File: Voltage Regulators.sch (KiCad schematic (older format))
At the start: 16 parts

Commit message: v1.0
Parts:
- added C?: 10n, symbol C_Small
- added C? (x2): 1u, symbol C_Small
- added U?: NCP700B, TSOT-23-5, symbol NCP700B
- C?: value 22n -> 100n
- R?: value 54.9k -> 43k
- R?: value 5k -> 3.9k
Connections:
- net +15V: now also D?.2 (A), L?.2
- net +3V3: now also C?.1, U?.5 (OUT); no longer C?.1, L?.1, U?.5 (Vin)
- net DC_3V6: now also C?.1, L?.1, U?.5 (Vin), C?.1, U?.1 (IN), U?.3 (EN)
- net GND: now also C?.2, C?.2, C?.2, U?.2 (GND)
- net at C?.2, D?.1 (K), L?.1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: no longer U?.16 (VSW)
- new net: C?.1, U?.4 (BYP)
- no-connect marks 3 -> 4
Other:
- note added: "EN pin mit uC verbinden\nEIngang vom Boost converter mit 3.3 oder 3.6 V verbinden?\n \n"
- note removed: "EN pin mit uC verbinden\n"
- moved on the sheet: C?, D?, L?, R?, U?

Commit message: Stand 10.03
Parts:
- added P?: CONN_01X02, Connectors_Phoenix:PhoenixContact_MSTBA-G_02x5.08mm_Angled, symbol CONN_01X02
- U?: footprint SOT-23-5 -> TO_SOT_Packages_SMD:TSOT-23-5
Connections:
- net DC_Vin: now also P?.2 (P2)
- net GND: now also P?.1 (P1)
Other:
- note added: "EN pin mit uC verbinden\n\n \n"
- note added: "FOOTPRINT not changed !"
- note removed: "EN pin mit uC verbinden\nEIngang vom Boost converter mit 3.3 oder 3.6 V verbinden?\n \n"
- moved on the sheet: C?, D?, L?, R?, U?

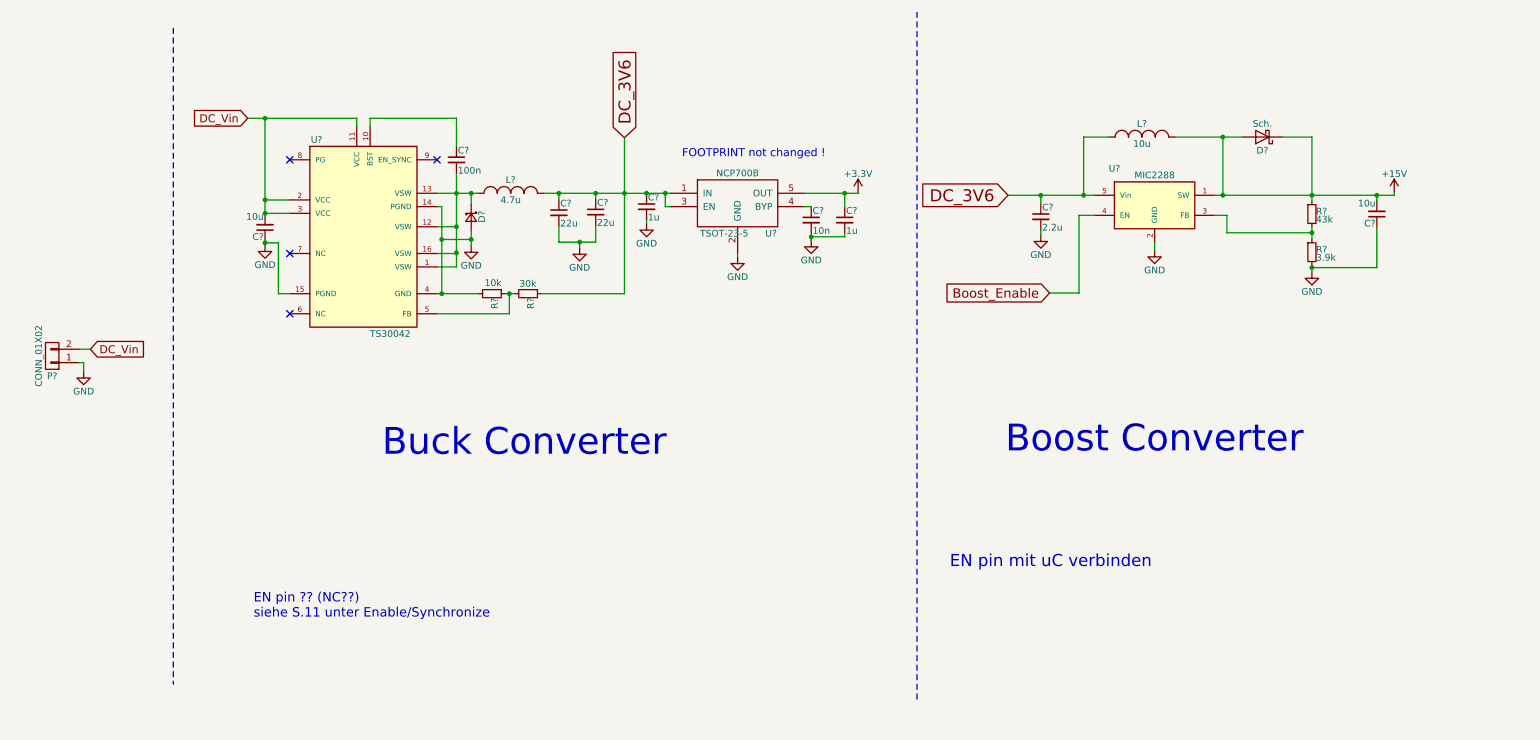
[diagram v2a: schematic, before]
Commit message: schematics ==> Check (exept BW) Layout started
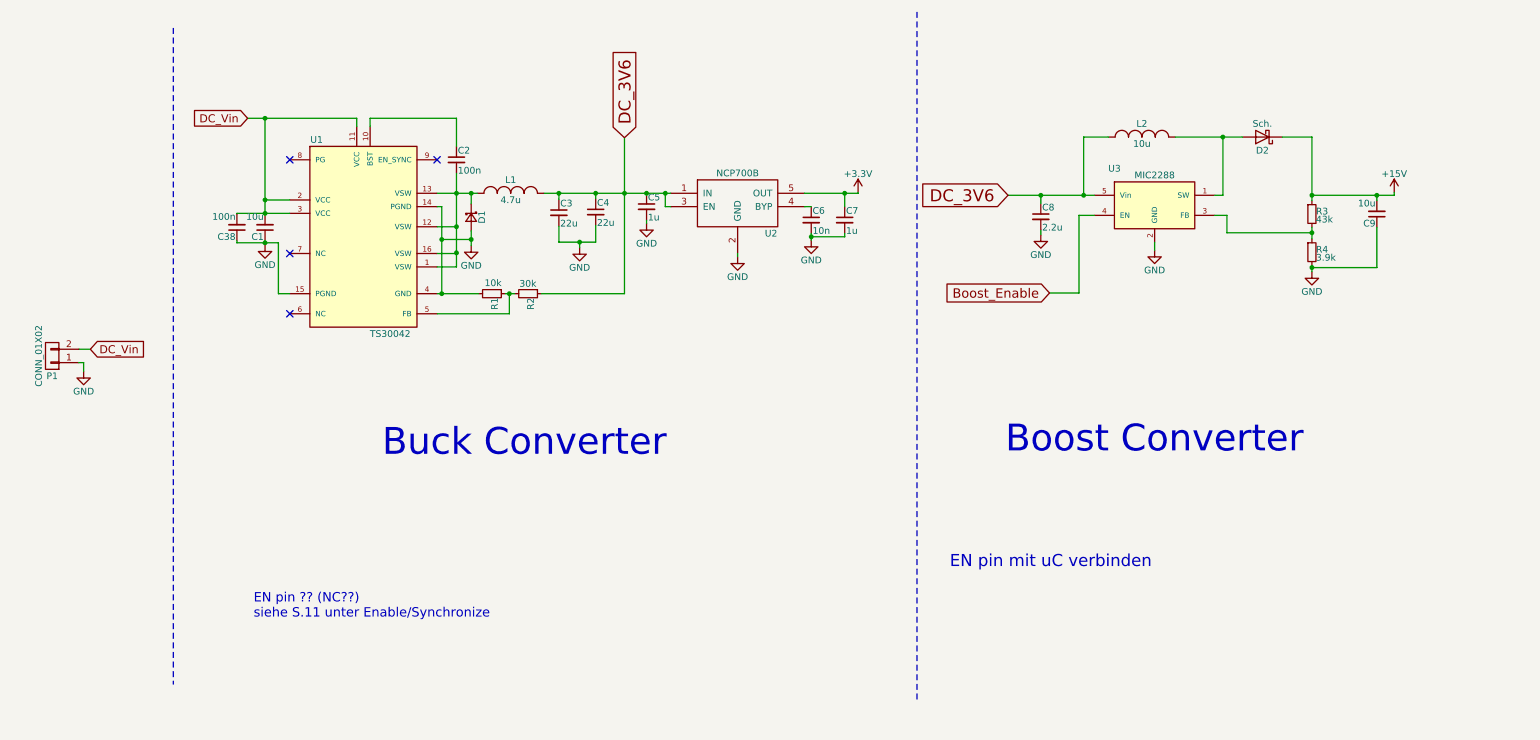
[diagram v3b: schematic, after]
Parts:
- removed D?: PMEG4030ER,115, symbol D_Schottky_Small
- added C38: 100n, Capacitors_SMD:C_0603, symbol C_Small
- added D1: D_Schottky_Small, .pretty:D_SOD-123, symbol D_Schottky_Small
- C1, C3, C4, C9: renamed from C?; footprint (none) -> Capacitors_SMD:C_1206
- C2, C5, C6, C7, C8: renamed from C?; footprint (none) -> Capacitors_SMD:C_0603
- D2: renamed from D?; footprint (none) -> .pretty:D_SOD-123
- L1: renamed from L?; footprint (none) -> Resistors_SMD:R_1210_HandSoldering; Mouser (none) -> LBC3225T4R7MR; RS (none) -> 786-6894
- L2: renamed from L?; footprint (none) -> Resistors_SMD:R_1210_HandSoldering; Mouser (none) -> LBC3225T100KR; RS (none) -> 786-6854
- R1, R2, R3, R4: renamed from R?; footprint (none) -> Resistors_SMD:R_0603
- U2: renamed from U?; footprint TSOT-23-5 -> Footprints:TSOP-5
- gave numbers to parts that had none: 3
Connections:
- net +15V: no longer D2.2 (A), L2.2, U3.1 (SW)
- net DC_Vin: now also C38.2
- net GND: now also C38.1, D1.2 (A)
- net at C2.2, L1.1, U1.1 (VSW)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: now also D1.1 (K)
- new net: D2.2 (A), L2.2, U3.1 (SW)
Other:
- note removed: "FOOTPRINT not changed !"

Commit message: added missing parts (SPI conn / Boost Conn/ drills..)
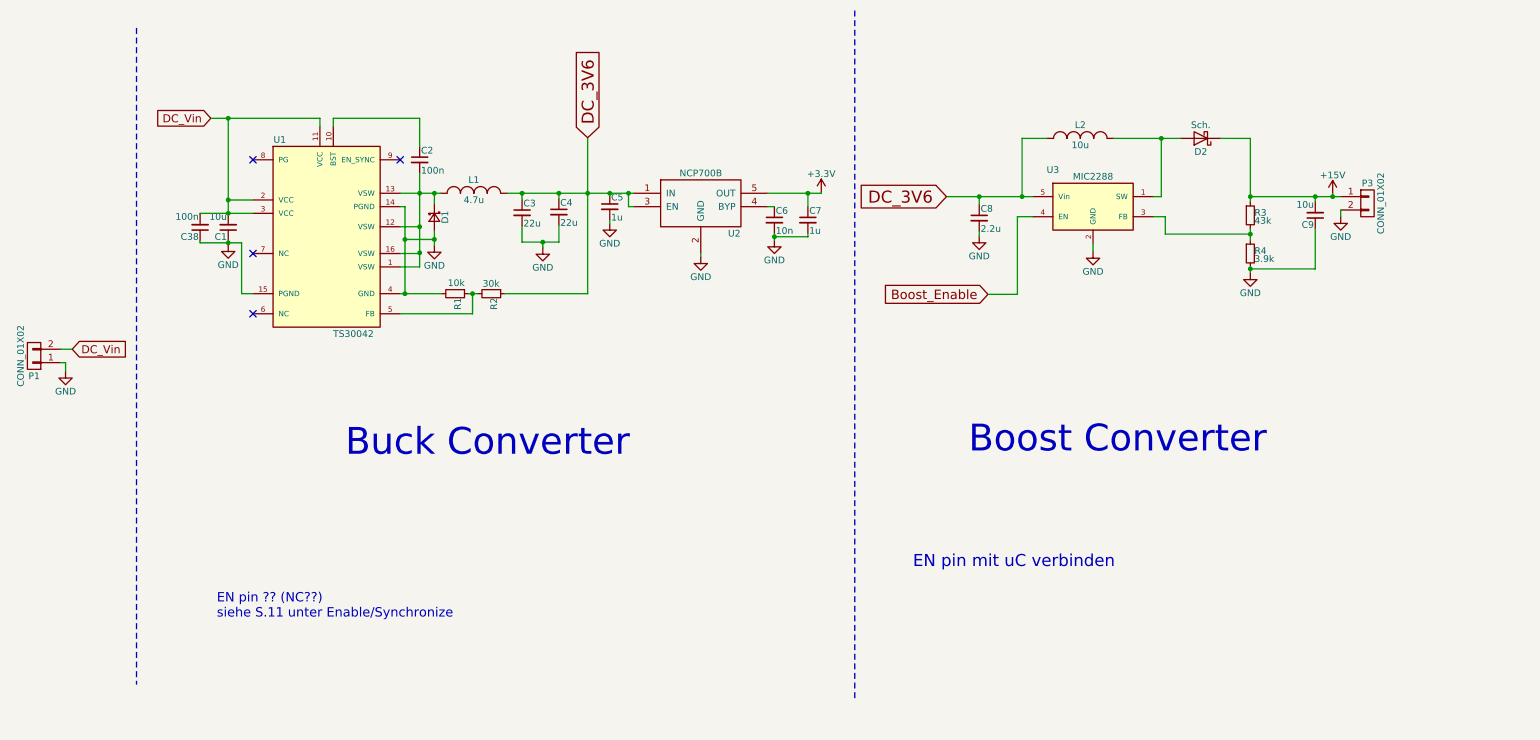
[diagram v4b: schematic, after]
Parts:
- added P3: CONN_01X02, Connectors_Phoenix:PhoenixContact_MSTBA-G_02x5.08mm_Angled, symbol CONN_01X02
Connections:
- net +15V: now also P3.1 (P1)
- net GND: now also P3.2 (P2)
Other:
- moved on the sheet: C1, C2, C3, C38, C4, C5, C6, C7, C8, C9, D1, D2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

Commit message: still the regulators & Planes fill
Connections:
- net at C2.2, D1.1 (K), L1.1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: now also U1.16 (VSW)

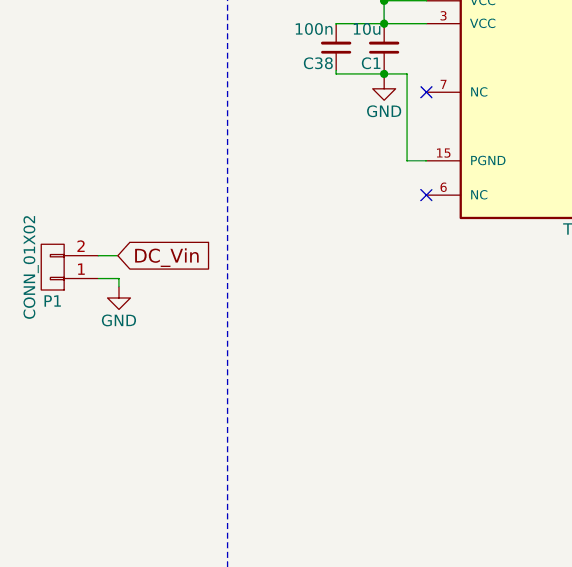
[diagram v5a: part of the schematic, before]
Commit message: routed the Buck & LDO ==> Still Boost
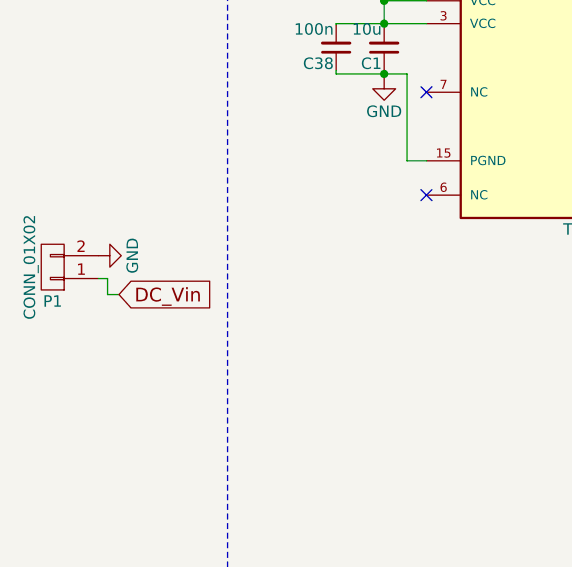
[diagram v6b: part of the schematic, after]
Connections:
- net DC_Vin: now also P1.1 (P1); no longer P1.2 (P2)
- net GND: now also P1.2 (P2); no longer P1.1 (P1)
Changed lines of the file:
@@
 	-1   0    0    1
 $EndComp
-Text GLabel 1070 3460 2    60   Input ~ 0
+Text GLabel 1075 3630 2    60   Input ~ 0
 DC_Vin
 $Comp
@@
 	1550 1060 1550 5965
 Wire Wire Line
-	1070 3460 985  3460
-Wire Wire Line
 	9870 2320 10545 2320
 Wire Wire Line
@@
 L GND #PWR012
 U 1 1 58C408F7
-P 1075 3595
-F 0 "#PWR012" H 1075 3345 50  0001 C CNN
-F 1 "GND" H 1075 3445 50  0000 C CNN
-F 2 "" H 1075 3595 50  0000 C CNN
-F 3 "" H 1075 3595 50  0000 C CNN
-	1    1075 3595
-	1    0    0    -1
-$EndComp
-Wire Wire Line
-	1075 3595 1075 3560
-Wire Wire Line
-	1075 3560 985  3560
+P 985 3460
+F 0 "#PWR012" H 985 3210 50  0001 C CNN
+F 1 "GND" H 985 3310 50  0000 C CNN
+F 2 "" H 985 3460 50  0000 C CNN
+F 3 "" H 985 3460 50  0000 C CNN
+	1    985  3460
+	0    -1   -1   0
+$EndComp
+Wire Wire Line
+	1075 3630 1025 3630
+Wire Wire Line
+	1025 3630 1025 3560
+Wire Wire Line
+	1025 3560 985  3560
 $EndSCHEMATC

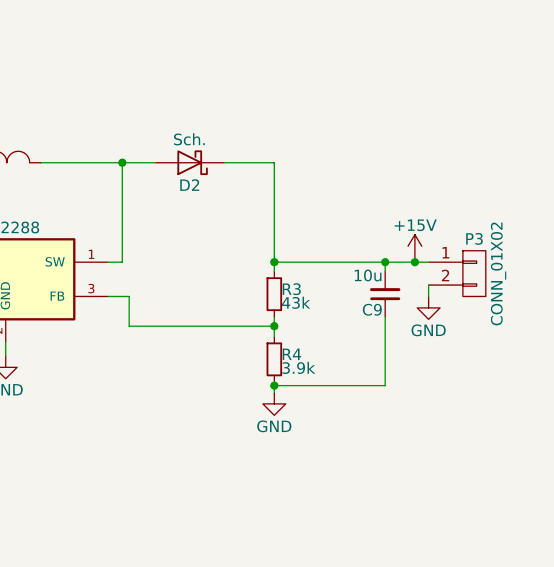
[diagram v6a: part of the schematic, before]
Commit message: connected Boost. Still inner layers
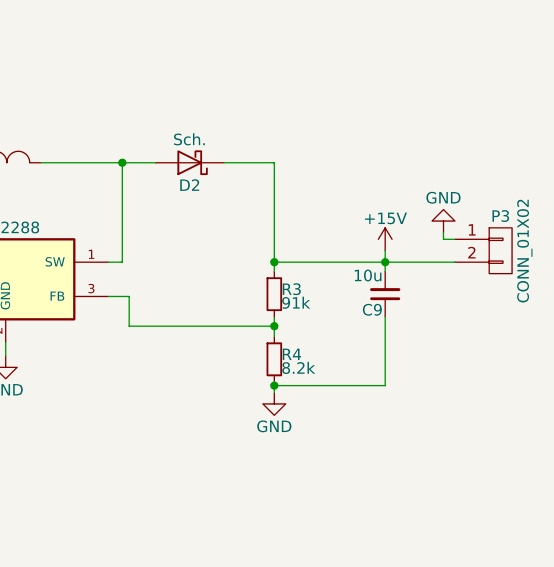
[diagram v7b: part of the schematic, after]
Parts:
- R3: value 43k -> 91k
- R4: value 3.9k -> 8.2k
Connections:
- net +15V: now also P3.2 (P2); no longer P3.1 (P1)
- net GND: now also P3.1 (P1); no longer P3.2 (P2)
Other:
- moved on the sheet: P3
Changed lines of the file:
@@
 P 9870 2460
 F 0 "R3" H 9900 2480 50  0000 L CNN
-F 1 "43k" H 9900 2420 50  0000 L CNN
+F 1 "91k" H 9900 2420 50  0000 L CNN
 F 2 "Resistors_SMD:R_0603" H 9870 2460 50  0001 C CNN
 F 3 "" H 9870 2460 50  0000 C CNN
@@
 P 9870 2745
 F 0 "R4" H 9900 2765 50  0000 L CNN
-F 1 "3.9k" H 9900 2705 50  0000 L CNN
+F 1 "8.2k" H 9900 2705 50  0000 L CNN
 F 2 "Resistors_SMD:R_0603" H 9870 2745 50  0001 C CNN
 F 3 "" H 9870 2745 50  0000 C CNN
@@
 L +15V #PWR06
 U 1 1 58B8B891
-P 10485 2300
-F 0 "#PWR06" H 10485 2150 50  0001 C CNN
-F 1 "+15V" H 10485 2440 50  0000 C CNN
-F 2 "" H 10485 2300 50  0000 C CNN
-F 3 "" H 10485 2300 50  0000 C CNN
-	1    10485 2300
+P 10355 2270
+F 0 "#PWR06" H 10355 2120 50  0001 C CNN
+F 1 "+15V" H 10355 2410 50  0000 C CNN
+F 2 "" H 10355 2270 50  0000 C CNN
+F 3 "" H 10355 2270 50  0000 C CNN
+	1    10355 2270
 	1    0    0    -1
 $EndComp
@@
 L CONN_01X02 P3
 U 1 1 58EF4649
-P 10745 2370
-F 0 "P3" H 10745 2520 50  0000 C CNN
-F 1 "CONN_01X02" V 10845 2370 50  0000 C CNN
-F 2 "Connectors_Phoenix:PhoenixContact_MSTBA-G_02x5.08mm_Angled" H 10745 2370 50  0001 C CNN
-F 3 "" H 10745 2370 50  0000 C CNN
-	1    10745 2370
-	1    0    0    -1
-$EndComp
-$Comp
-L GND #PWR013
+P 10860 2270
+F 0 "P3" H 10860 2420 50  0000 C CNN
+F 1 "CONN_01X02" V 10960 2270 50  0000 C CNN
+F 2 "Connectors_Phoenix:PhoenixContact_MSTBA-G_02x5.08mm_Angled" H 10860 2270 50  0001 C CNN
+F 3 "" H 10860 2270 50  0000 C CNN
+	1    10860 2270
+	1    0    0    -1
+$EndComp
+$Comp
+L GND #PWR012
 U 1 1 58EF65A8
-P 10545 2470
-F 0 "#PWR013" H 10545 2220 50  0001 C CNN
-F 1 "GND" H 10545 2320 50  0000 C CNN
-F 2 "" H 10545 2470 50  0000 C CNN
-F 3 "" H 10545 2470 50  0000 C CNN
-	1    10545 2470
-	1    0    0    -1
+P 10610 2190
+F 0 "#PWR012" H 10610 1940 50  0001 C CNN
+F 1 "GND" H 10610 2040 50  0000 C CNN
+F 2 "" H 10610 2190 50  0000 C CNN
+F 3 "" H 10610 2190 50  0000 C CNN
+	1    10610 2190
+	-1   0    0    1
 $EndComp
 Connection ~ 6565 2295
@@
 	9650 1885 9870 1885
 Wire Wire Line
-	10485 2320 10485 2300
-Wire Wire Line
 	7845 2615 7845 2580
 Connection ~ 7845 2320
@@
 	9870 2560 9870 2645
 Wire Wire Line
-	10355 2320 10355 2360
+	10355 2270 10355 2360
 Wire Notes Line
 	6915 930  6915 6090
@@
 	1550 1060 1550 5965
 Wire Wire Line
-	9870 2320 10545 2320
+	9870 2320 10660 2320
 Wire Wire Line
 	9870 1885 9870 2360
@@
 Wire Wire Line
 	2025 2650 2025 2665
-Connection ~ 10485 2320
-Wire Wire Line
-	10545 2470 10545 2420
 Wire Wire Line
 	3520 2745 3665 2745
 Connection ~ 3665 2745
 $Comp
-L GND #PWR012
+L GND #PWR013
 U 1 1 58C408F7
 P 985 3460
-F 0 "#PWR012" H 985 3210 50  0001 C CNN
+F 0 "#PWR013" H 985 3210 50  0001 C CNN
 F 1 "GND" H 985 3310 50  0000 C CNN
 F 2 "" H 985 3460 50  0000 C CNN
@@
 Wire Wire Line
 	1025 3560 985  3560
+Wire Wire Line
+	10660 2220 10610 2220
+Wire Wire Line
+	10610 2220 10610 2190
 $EndSCHEMATC
